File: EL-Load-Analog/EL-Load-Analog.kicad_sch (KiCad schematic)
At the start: 9 parts, among them J1 Temp Sensor PCB, J9 Temp Sensor heatsink, Q101 TIP42C, Q4 MMBT3904

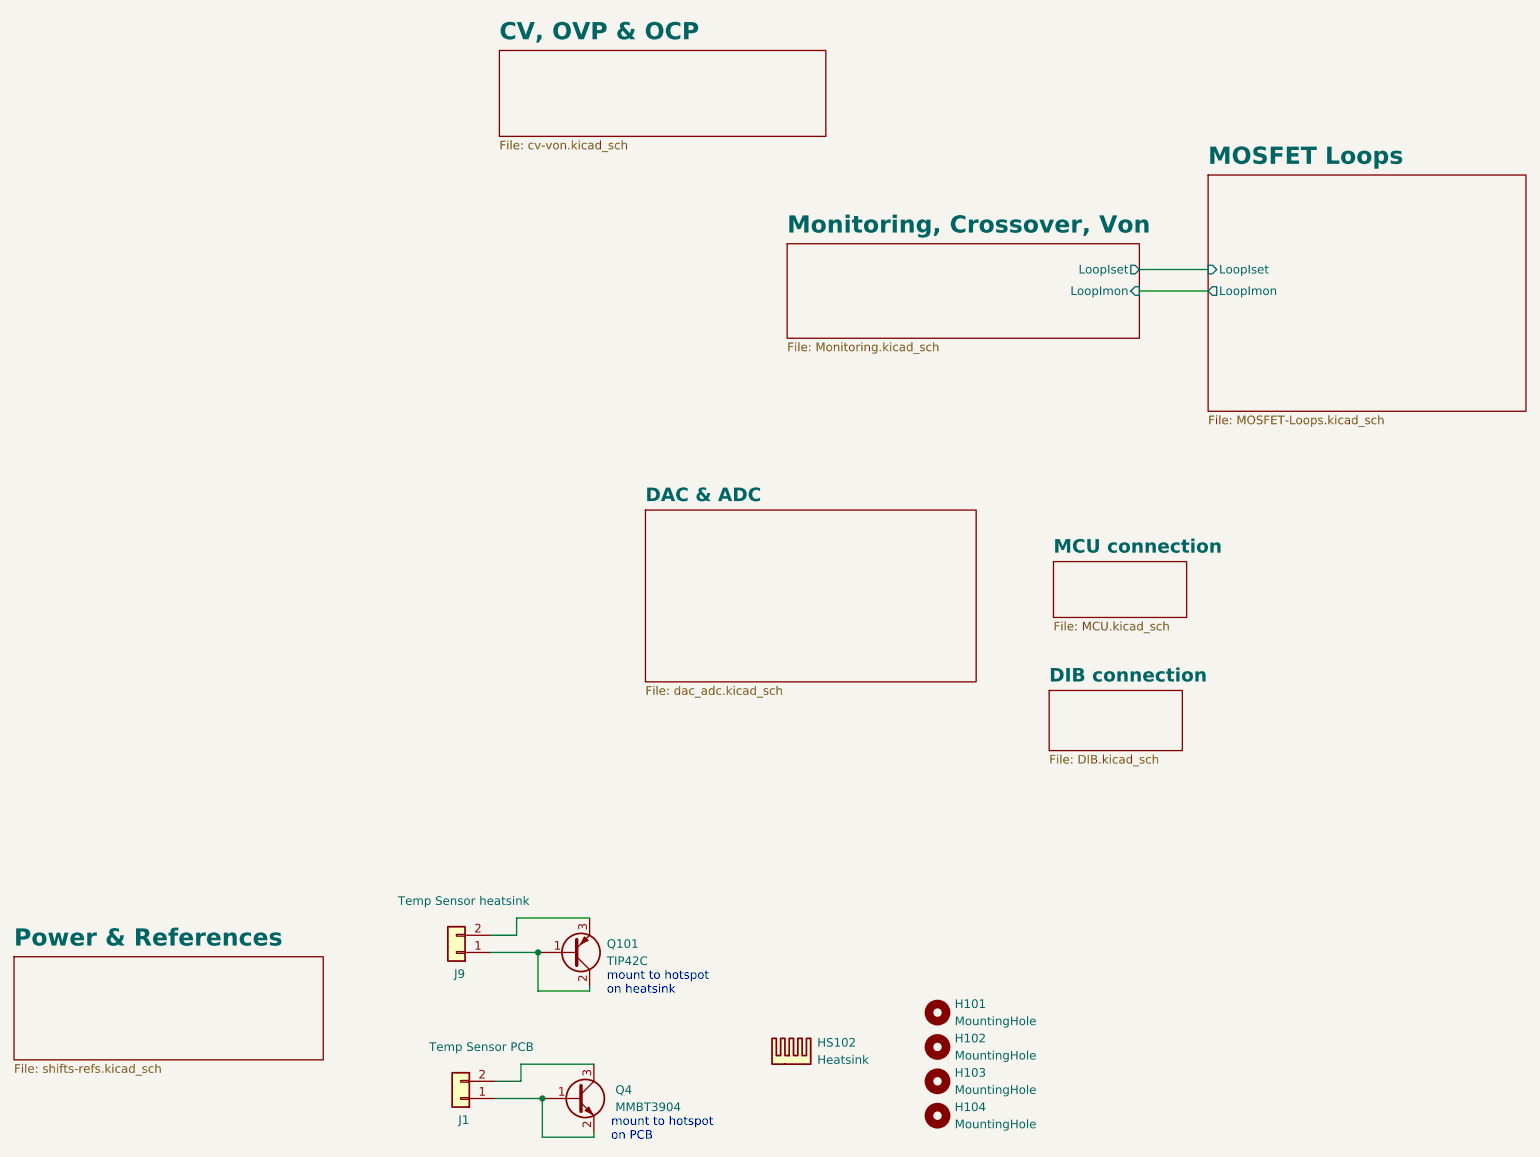
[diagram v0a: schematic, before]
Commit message: Added heatsink moutingholes, reverse polarity, moved snubbers.
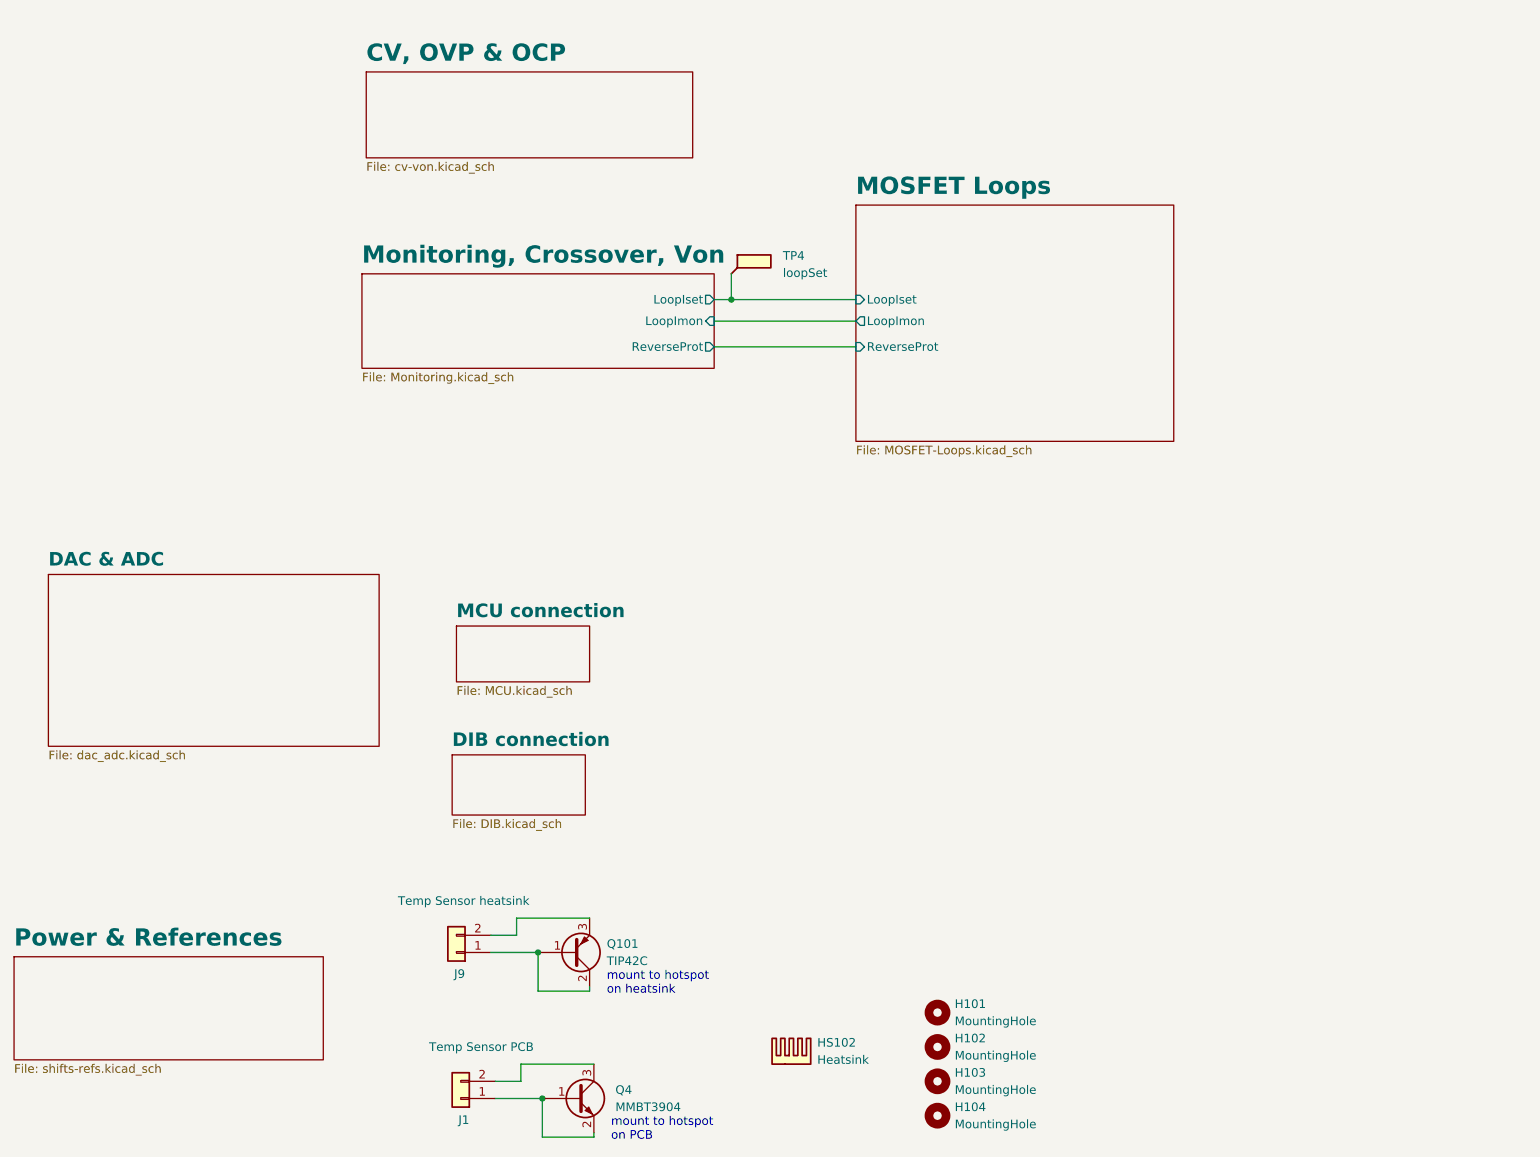
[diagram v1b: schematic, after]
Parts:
- added TP4: loopSet, TestPoint:TestPoint_Pad_1.0x1.0mm, symbol Connector:TestPoint_Flag
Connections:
- net MOSFET Loops/LoopIset: now also TP4.1
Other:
- sheet MOSFET Loops ports: added ReverseProt; removed none
- sheet Monitoring, Crossover, Von ports: added ReverseProt; removed none
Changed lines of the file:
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@@
   (junction (at 99.06 189.23) (diameter 0) (color 0 0 0 0)
   )
+  (junction (at 127 71.12) (diameter 0) (color 0 0 0 0)
+  )
   (junction (at 98.425 167.64) (diameter 0) (color 0 0 0 0)
   )
@@
     (stroke (width 0) (type default))
   )
+  (wire (pts (xy 124.46 78.105) (xy 145.415 78.105))
+    (stroke (width 0) (type default))
+  )
   (wire (pts (xy 106.68 184.15) (xy 95.885 184.15))
     (stroke (width 0) (type default))
   )
-  (wire (pts (xy 187.325 66.675) (xy 197.485 66.675))
+  (wire (pts (xy 124.46 71.12) (xy 127 71.12))
     (stroke (width 0) (type default))
   )
@@
     (stroke (width 0) (type default))
   )
+  (wire (pts (xy 127 71.12) (xy 145.415 71.12))
+    (stroke (width 0) (type default))
+  )
+  (wire (pts (xy 127 67.31) (xy 127 71.12))
+    (stroke (width 0) (type default))
+  )
   (wire (pts (xy 99.06 189.23) (xy 99.06 194.945))
     (stroke (width 0) (type default))
   )
-  (wire (pts (xy 187.325 69.85) (xy 197.485 69.85))
+  (wire (pts (xy 124.46 74.295) (xy 145.415 74.295))
     (stroke (width 0) (type default))
   )
@@
     )
   )
+  (symbol (lib_id "Connector:TestPoint_Flag") (at 127 67.31 0) (unit 1)
+    (in_bom yes) (on_board yes) (dnp no) (fields_autoplaced)
+    (property "Reference" "TP4" (at 134.62 64.643 0)
+      (effects (font (size 1.27 1.27)) (justify left))
+    )
+    (property "Value" "loopSet" (at 134.62 67.183 0)
+      (effects (font (size 1.27 1.27)) (justify left))
+    )
+    (property "Footprint" "TestPoint:TestPoint_Pad_1.0x1.0mm" (at 132.08 67.31 0)
+      (effects (font (size 1.27 1.27)) hide)
+    )
+    (property "Datasheet" "~" (at 132.08 67.31 0)
+      (effects (font (size 1.27 1.27)) hide)
+    )
+    (pin "1")
+    (instances
+      (project "EL-Load-Analog"
+        (path "/51d9228f-95b8-4f0d-bdba-83c3975c517c/8af1df1b-1025-4aef-94e0-10ff3284a07d"
+          (reference "TP4") (unit 1)
+        )
+        (path "/51d9228f-95b8-4f0d-bdba-83c3975c517c"
+          (reference "TP14") (unit 1)
+        )
+      )
+    )
+  )
   (symbol (lib_id "Connector_Generic:Conn_01x02") (at 86.36 167.64 180) (unit 1)
     (in_bom yes) (on_board yes) (dnp no)
@@
     )
   )
-  (sheet (at 173.99 128.905) (size 19.685 8.89) (fields_autoplaced)
-    (stroke (width 0.1524) (type solid))
-    (fill (color 0 0 0 0.0000))
-    (property "Sheetname" "DIB connection" (at 173.99 127.8284 0)
+  (sheet (at 85.725 138.43) (size 19.685 8.89) (fields_autoplaced)
+    (stroke (width 0.1524) (type solid))
+    (fill (color 0 0 0 0.0000))
+    (property "Sheetname" "DIB connection" (at 85.725 137.3534 0)
       (effects (font (size 2 2) bold) (justify left bottom))
     )
-    (property "Sheetfile" "DIB.kicad_sch" (at 173.99 138.3796 0)
+    (property "Sheetfile" "DIB.kicad_sch" (at 85.725 147.9046 0)
       (effects (font (size 1.27 1.27)) (justify left top))
     )
@@
     )
   )
-  (sheet (at 174.625 109.855) (size 19.685 8.255) (fields_autoplaced)
-    (stroke (width 0.1524) (type solid))
-    (fill (color 0 0 0 0.0000))
-    (property "Sheetname" "MCU connection" (at 174.625 108.7784 0)
+  (sheet (at 86.36 119.38) (size 19.685 8.255) (fields_autoplaced)
+    (stroke (width 0.1524) (type solid))
+    (fill (color 0 0 0 0.0000))
+    (property "Sheetname" "MCU connection" (at 86.36 118.3034 0)
       (effects (font (size 2 2) bold) (justify left bottom))
     )
-    (property "Sheetfile" "MCU.kicad_sch" (at 174.625 118.6946 0)
+    (property "Sheetfile" "MCU.kicad_sch" (at 86.36 128.2196 0)
       (effects (font (size 1.27 1.27)) (justify left top))
     )
@@
     )
   )
-  (sheet (at 92.71 34.29) (size 48.26 12.7) (fields_autoplaced)
-    (stroke (width 0.1524) (type solid))
-    (fill (color 0 0 0 0.0000))
-    (property "Sheetname" "CV, OVP & OCP" (at 92.71 32.9434 0)
+  (sheet (at 73.025 37.465) (size 48.26 12.7) (fields_autoplaced)
+    (stroke (width 0.1524) (type solid))
+    (fill (color 0 0 0 0.0000))
+    (property "Sheetname" "CV, OVP & OCP" (at 73.025 36.1184 0)
       (effects (font (size 2.54 2.54) bold) (justify left bottom))
     )
-    (property "Sheetfile" "cv-von.kicad_sch" (at 92.71 47.5746 0)
+    (property "Sheetfile" "cv-von.kicad_sch" (at 73.025 50.7496 0)
       (effects (font (size 1.27 1.27)) (justify left top))
     )
@@
     )
   )
-  (sheet (at 135.255 62.865) (size 52.07 13.97) (fields_autoplaced)
-    (stroke (width 0.1524) (type solid))
-    (fill (color 0 0 0 0.0000))
-    (property "Sheetname" "Monitoring, Crossover, Von" (at 135.255 61.5184 0)
+  (sheet (at 72.39 67.31) (size 52.07 13.97) (fields_autoplaced)
+    (stroke (width 0.1524) (type solid))
+    (fill (color 0 0 0 0.0000))
+    (property "Sheetname" "Monitoring, Crossover, Von" (at 72.39 65.9634 0)
       (effects (font (size 2.54 2.54) bold) (justify left bottom))
     )
-    (property "Sheetfile" "Monitoring.kicad_sch" (at 135.255 77.4196 0)
-      (effects (font (size 1.27 1.27)) (justify left top))
-    )
-    (pin "LoopIset" output (at 187.325 66.675 0)
+    (property "Sheetfile" "Monitoring.kicad_sch" (at 72.39 81.8646 0)
+      (effects (font (size 1.27 1.27)) (justify left top))
+    )
+    (pin "LoopIset" output (at 124.46 71.12 0)
       (effects (font (size 1.27 1.27)) (justify right))
     )
-    (pin "LoopImon" input (at 187.325 69.85 0)
+    (pin "LoopImon" input (at 124.46 74.295 0)
       (effects (font (size 1.27 1.27)) (justify right))
     )
+    (pin "ReverseProt" output (at 124.46 78.105 0)
+      (effects (font (size 1.27 1.27)) (justify right))
+    )
     (instances
       (project "EL-Load-Analog"
@@
     )
   )
-  (sheet (at 197.485 52.705) (size 46.99 34.925) (fields_autoplaced)
-    (stroke (width 0.1524) (type solid))
-    (fill (color 0 0 0 0.0000))
-    (property "Sheetname" "MOSFET Loops" (at 197.485 51.3584 0)
+  (sheet (at 145.415 57.15) (size 46.99 34.925) (fields_autoplaced)
+    (stroke (width 0.1524) (type solid))
+    (fill (color 0 0 0 0.0000))
+    (property "Sheetname" "MOSFET Loops" (at 145.415 55.8034 0)
       (effects (font (size 2.54 2.54) bold) (justify left bottom))
     )
-    (property "Sheetfile" "MOSFET-Loops.kicad_sch" (at 197.485 88.2146 0)
-      (effects (font (size 1.27 1.27)) (justify left top))
-    )
-    (pin "LoopIset" input (at 197.485 66.675 180)
-      (effects (font (size 1.27 1.27)) (justify left))
-    )
-    (pin "LoopImon" output (at 197.485 69.85 180)
+    (property "Sheetfile" "MOSFET-Loops.kicad_sch" (at 145.415 92.6596 0)
+      (effects (font (size 1.27 1.27)) (justify left top))
+    )
+    (pin "LoopIset" input (at 145.415 71.12 180)
+      (effects (font (size 1.27 1.27)) (justify left))
+    )
+    (pin "LoopImon" output (at 145.415 74.295 180)
+      (effects (font (size 1.27 1.27)) (justify left))
+    )
+    (pin "ReverseProt" input (at 145.415 78.105 180)
       (effects (font (size 1.27 1.27)) (justify left))
     )
@@
     )
   )
-  (sheet (at 114.3 102.235) (size 48.895 25.4) (fields_autoplaced)
-    (stroke (width 0.1524) (type solid))
-    (fill (color 0 0 0 0.0000))
-    (property "Sheetname" "DAC & ADC" (at 114.3 101.1584 0)
+  (sheet (at 26.035 111.76) (size 48.895 25.4) (fields_autoplaced)
+    (stroke (width 0.1524) (type solid))
+    (fill (color 0 0 0 0.0000))
+    (property "Sheetname" "DAC & ADC" (at 26.035 110.6834 0)
       (effects (font (size 2 2) bold) (justify left bottom))
     )
-    (property "Sheetfile" "dac_adc.kicad_sch" (at 114.3 128.2196 0)
-      (effects (font (size 1.27 1.27)) (justify left top))
-    )
+    (property "Sheetfile" "dac_adc.kicad_sch" (at 26.035 137.7446 0)
+      (effects (font (size 1.27 1.27)) (justify left top))
+    )
